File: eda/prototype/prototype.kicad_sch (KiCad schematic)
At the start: 9 parts, among them U1 8088_Min_Mode, U2 GAL16V8, U3 74HC161, U4 74HC574, U5 SST39SF040, U6 HM62256BLP, U7 HM62256BLP, U8 74HC245, X1 CXO_DIP8

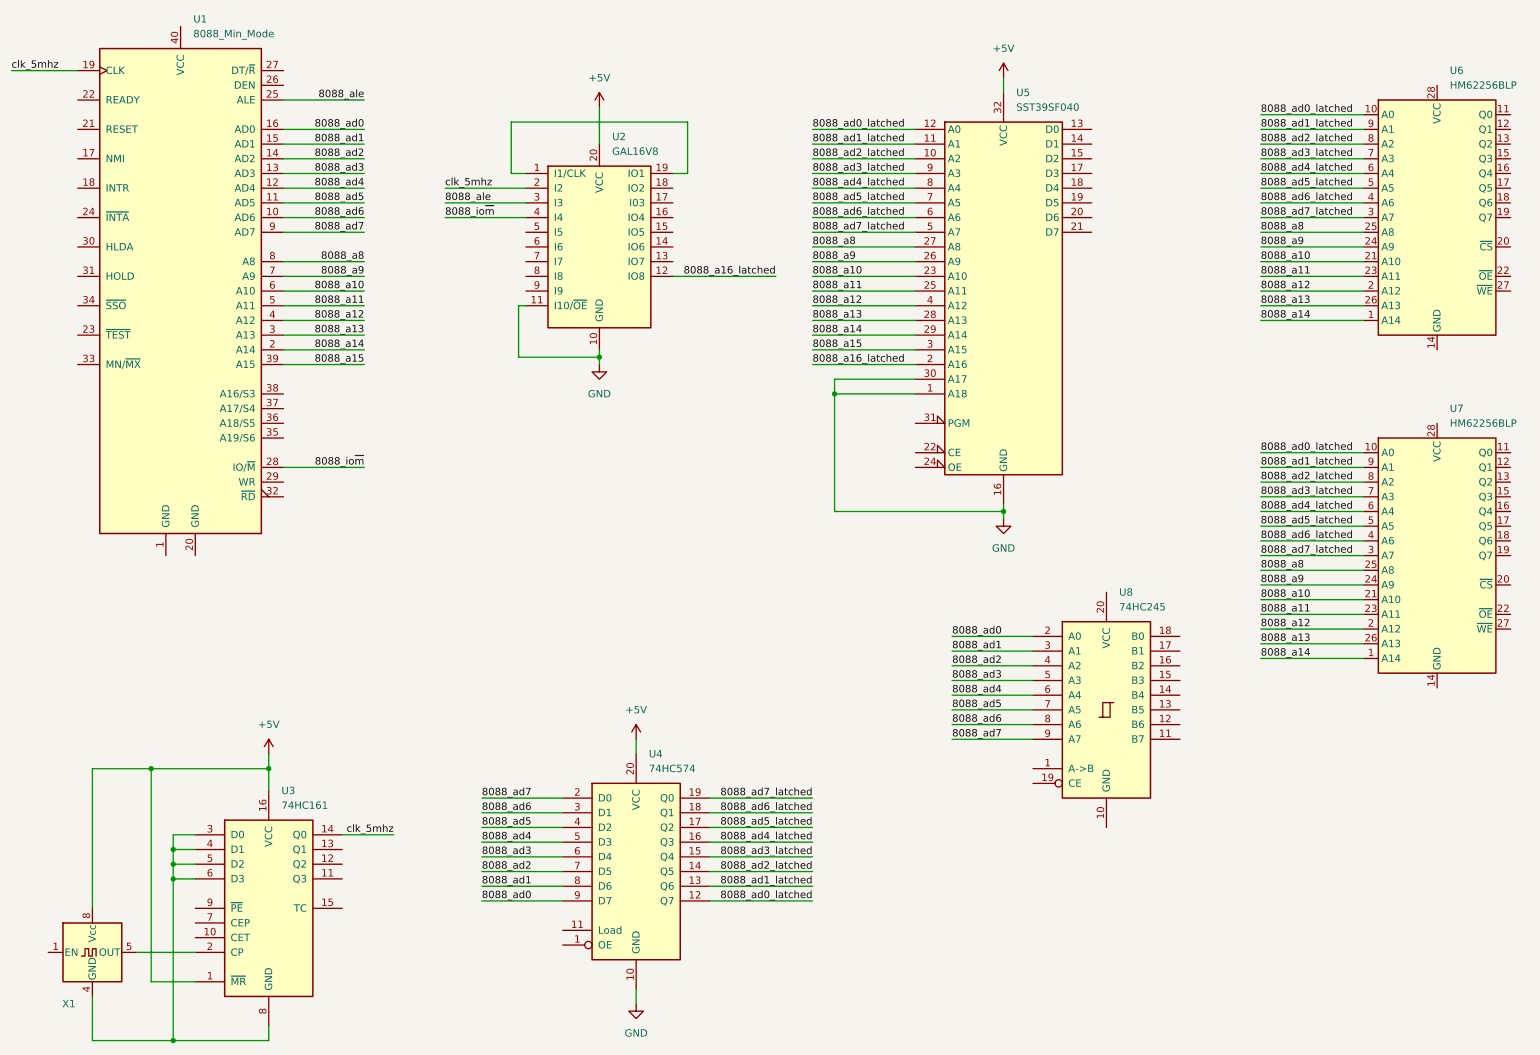
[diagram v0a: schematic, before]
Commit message: eda: Mostly complete prototype schematic
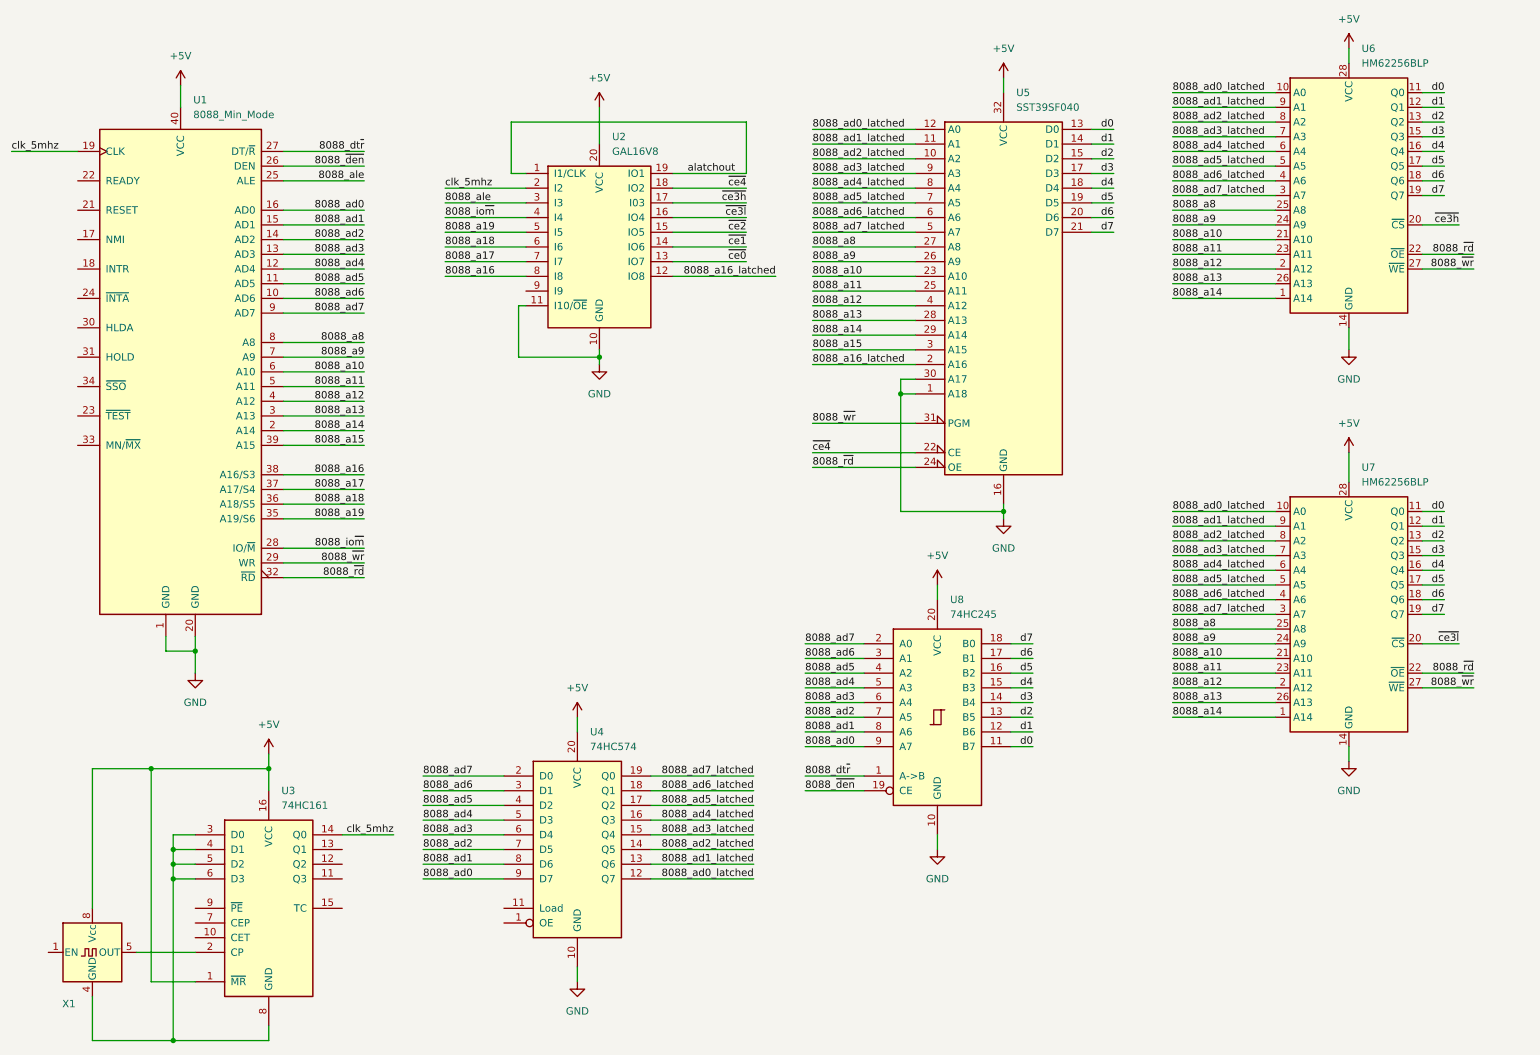
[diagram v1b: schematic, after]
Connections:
- net +5V: now also U1.40 (VCC), U6.28 (VCC), U7.28 (VCC), U8.20 (VCC)
- net 8088_ad0: now also U8.9 (A7); no longer U8.2 (A0)
- net 8088_ad1: now also U8.8 (A6); no longer U8.3 (A1)
- net 8088_ad2: now also U8.7 (A5); no longer U8.4 (A2)
- net 8088_ad3: now also U8.6 (A4); no longer U8.5 (A3)
- net 8088_ad4: now also U8.5 (A3); no longer U8.6 (A4)
- net 8088_ad5: now also U8.4 (A2); no longer U8.7 (A5)
- net 8088_ad6: now also U8.3 (A1); no longer U8.8 (A6)
- net 8088_ad7: now also U8.2 (A0); no longer U8.9 (A7)
- net GND: now also U1.1 (GND), U1.20 (GND), U6.14 (GND), U7.14 (GND), U8.10 (GND)
- net d0: now reaches U5.13 (D0)
- net d0: now also U6.11 (Q0), U7.11 (Q0), U8.11 (B7)
- net d1: now reaches U5.14 (D1)
- net d1: now also U6.12 (Q1), U7.12 (Q1), U8.12 (B6)
- net d2: now reaches U5.15 (D2)
- net d2: now also U6.13 (Q2), U7.13 (Q2), U8.13 (B5)
- net d3: now reaches U5.17 (D3)
- net d3: now also U6.15 (Q3), U7.15 (Q3), U8.14 (B4)
- net d4: now reaches U5.18 (D4)
- net d4: now also U6.16 (Q4), U7.16 (Q4), U8.15 (B3)
- net d5: now reaches U5.19 (D5)
- net d5: now also U6.17 (Q5), U7.17 (Q5), U8.16 (B2)
- net d6: now reaches U5.20 (D6)
- net d6: now also U6.18 (Q6), U7.18 (Q6), U8.17 (B1)
- net d7: now reaches U5.21 (D7)
- net d7: now also U6.19 (Q7), U7.19 (Q7), U8.18 (B0)
- net ~{ce4}: now reaches U5.22 (CE)
- net ~{ce4}: now also U2.18 (IO2)
- net 8088_~{rd}: now reaches U5.24 (OE)
- net 8088_~{rd}: now also U1.32 (~{RD}), U6.22 (~{OE}), U7.22 (~{OE})
- net 8088_~{wr}: now reaches U5.31 (PGM)
- net 8088_~{wr}: now also U1.29 (WR), U6.27 (~{WE}), U7.27 (~{WE})
- net 8088_dt~{r}: now reaches U8.1 (A->B)
- net 8088_dt~{r}: now also U1.27 (DT/~{R})
- net 8088_~{den}: now reaches U8.19 (CE)
- net 8088_~{den}: now also U1.26 (DEN)
- net alatchout: now reaches U2.1 (I1/CLK), U2.19 (IO1)
- net ~{ce0}: now reaches U2.13 (IO7)
- net ~{ce1}: now reaches U2.14 (IO6)
- net ~{ce2}: now reaches U2.15 (IO5)
- net ~{ce3l}: now reaches U2.16 (IO4)
- net ~{ce3l}: now also U7.20 (~{CS})
- net ~{ce3h}: now reaches U2.17 (I03)
- net ~{ce3h}: now also U6.20 (~{CS})
- net 8088_a19: now reaches U2.5 (I5)
- net 8088_a19: now also U1.35 (A19/S6)
- net 8088_a18: now reaches U2.6 (I6)
- net 8088_a18: now also U1.36 (A18/S5)
- net 8088_a17: now reaches U2.7 (I7)
- net 8088_a17: now also U1.37 (A17/S4)
- net 8088_a16: now reaches U2.8 (I8)
- net 8088_a16: now also U1.38 (A16/S3)
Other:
- moved on the sheet: U1, U4, U6, U7, U8

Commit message: eda: prototype: bit more filling out
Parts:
- added R1, R2, R3, R4, R5, R6, R7: R, symbol Device:R
- added U9: GAL16V8, symbol Logic_Programmable:GAL16V8
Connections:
- net +5V: now also R3.1, R4.1, R7.1, U9.20 (VCC)
- net 8088_a12: now also U9.3 (I3)
- net 8088_a13: now also U9.4 (I4)
- net 8088_a14: now also U9.5 (I5)
- net 8088_a15: now also U9.6 (I6)
- net 8088_io~{m}: now also U9.2 (I2)
- net GND: now also U4.1 (OE), R1.1, R2.2, R5.2, R6.2, U9.10 (GND), U9.11 (I10/~{OE})
- net alatchout: now also U4.11 (Load), U9.1 (I1/CLK)
- net at U1.17 (NMI): now also R1.2
- net at U1.18 (INTR): now also R6.1
- net at U1.21 (RESET): now also R4.2
- net at U1.22 (READY): now also R7.2
- net at U1.23 (~{TEST}): now also R5.1
- net at U1.31 (HOLD): now also R2.1
- net at U1.33 (MN/~{MX}): now also R3.2
- new net ~{ioce0}: U9.12 (IO8)
- new net ~{ioce1}: U9.13 (IO7)
- new net ~{ioce2}: U9.14 (IO6)
- new net ~{ioce3}: U9.15 (IO5)
- new net ~{ioce4}: U9.16 (IO4)
- new net ~{ioce5}: U9.17 (I03)
- new net ~{ioce6}: U9.18 (IO2)
- new net ~{ioce7}: U9.19 (IO1)
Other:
- moved on the sheet: U1, U2, U4, U5, U6, U7, U8

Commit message: eda: prototype: Add pio
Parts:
- added U10: 8255A, Package_DIP:DIP-40_W15.24mm, symbol Interface:8255A
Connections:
- net ~{ioce7} is gone; now on net 8088_io~{m}: U9.19 (IO1)
- net 8088_a12: now also U9.6 (I6); no longer U9.3 (I3)
- net 8088_a13: now also U9.7 (I7); no longer U9.4 (I4)
- net 8088_a14: now also U9.8 (I8); no longer U9.5 (I5)
- net 8088_a15: now also U9.9 (I9); no longer U9.6 (I6)
- net 8088_ad0_latched: now also U10.8 (A1)
- net 8088_ad1_latched: now also U10.9 (A0)
- net 8088_ad4: now also U9.5 (I5)
- net 8088_ad5: now also U9.4 (I4)
- net 8088_ad6: now also U9.3 (I3)
- net 8088_ad7: now also U9.2 (I2)
- net 8088_io~{m}: no longer U9.2 (I2)
- net 8088_~{rd}: now also U10.5 (~{RD})
- net 8088_~{wr}: now also U10.36 (~{WR})
- net GND: now also U10.7 (GND)
- net d0: now also U10.34 (D0)
- net d1: now also U10.33 (D1)
- net d2: now also U10.32 (D2)
- net d3: now also U10.31 (D3)
- net d4: now also U10.30 (D4)
- net d5: now also U10.29 (D5)
- net d6: now also U10.28 (D6)
- net d7: now also U10.27 (D7)
- net ~{ioce0}: now also U10.6 (~{CS})
- net reset: now reaches R4.2, U1.21 (RESET)
- net reset: now also U10.35 (RESET)
- net ~{ioce6} renamed ~{iodbg}
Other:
- moved on the sheet: U9

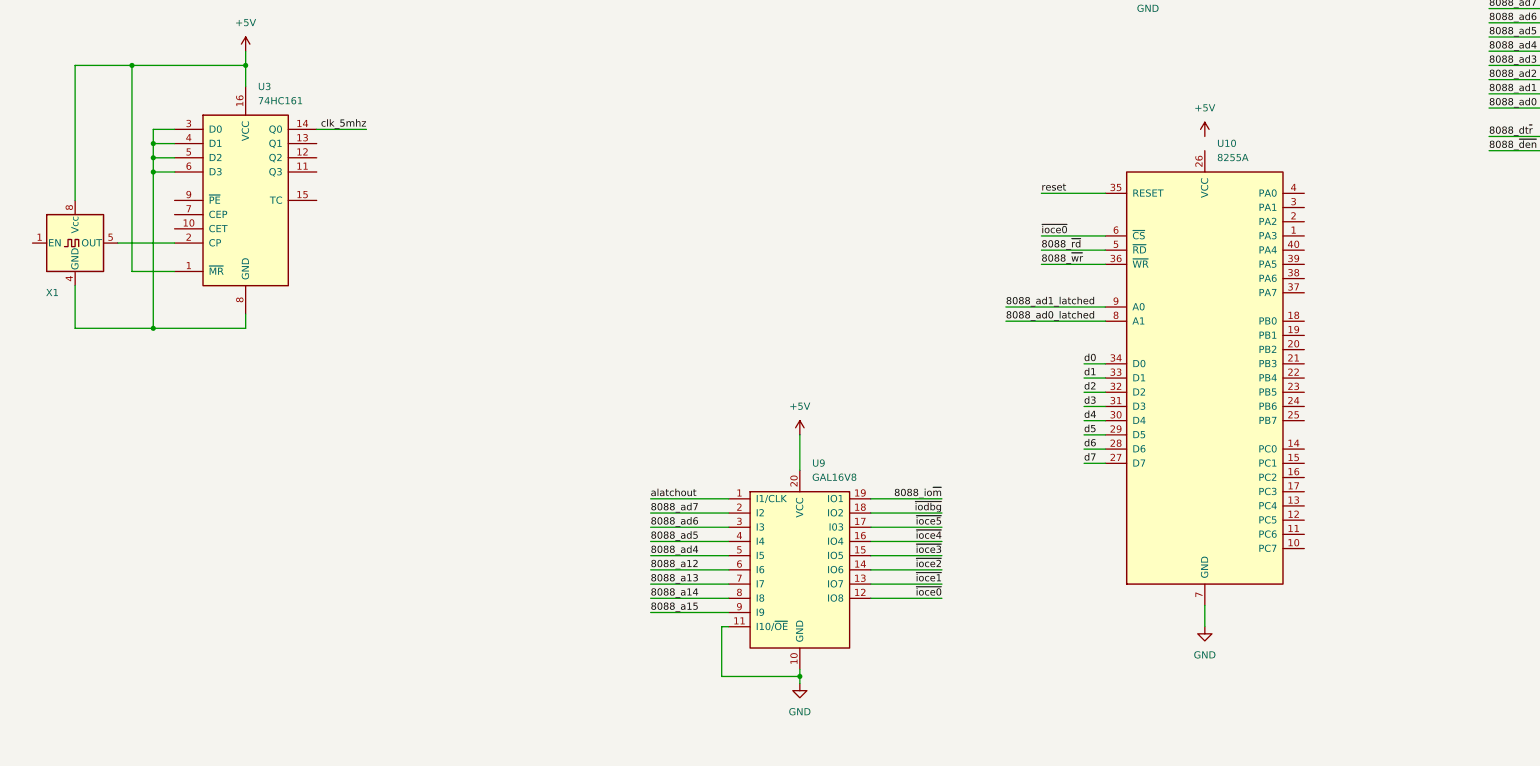
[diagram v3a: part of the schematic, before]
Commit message: eda: prototype: Update schematic
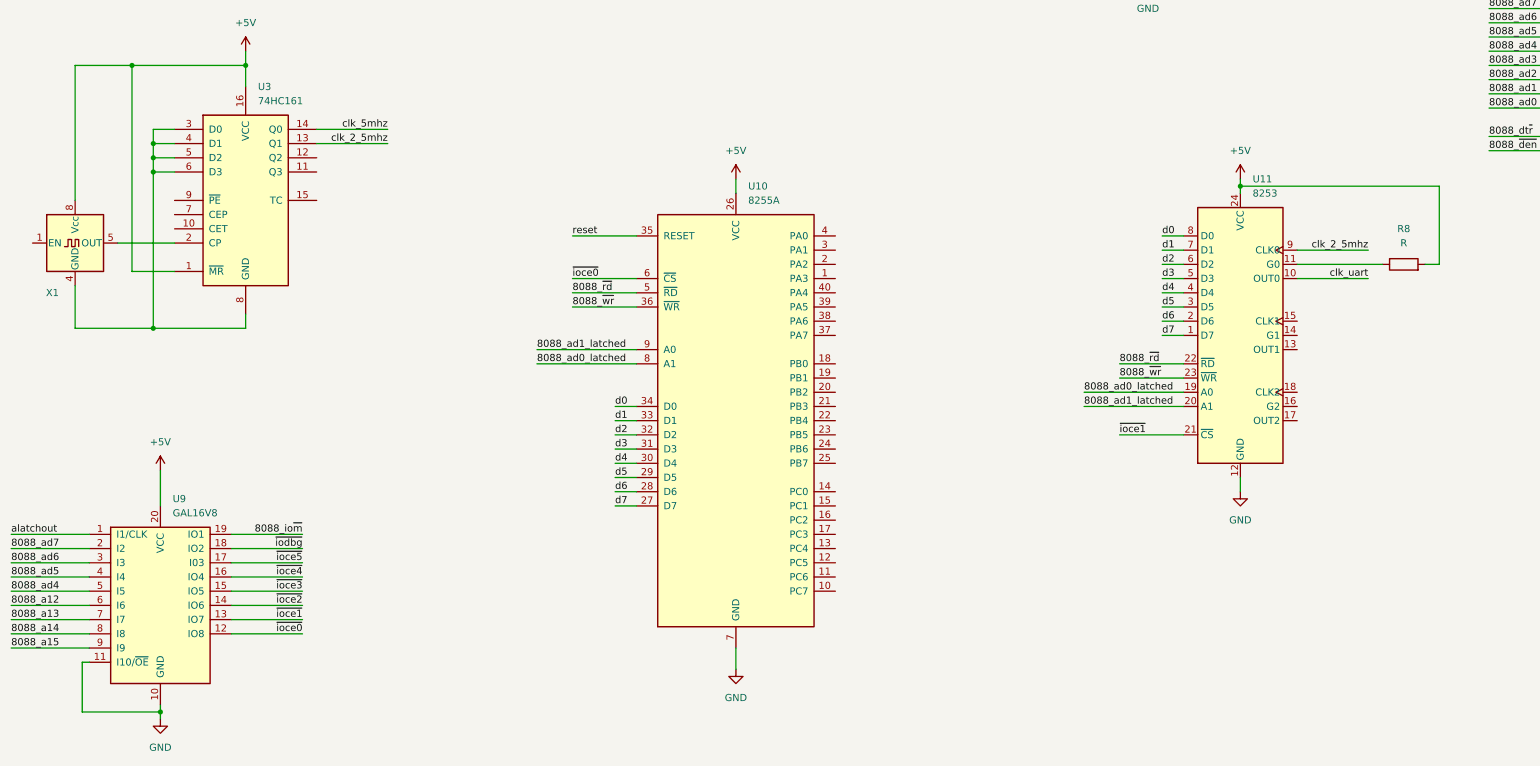
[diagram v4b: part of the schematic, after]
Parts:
- added R8: R, symbol Device:R
- added U11: 8253, Package_DIP:DIP-24_W15.24mm, symbol Timer:8253
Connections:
- net +5V: now also U10.26 (VCC), R8.2, U11.24 (VCC)
- net 8088_ad0_latched: now also U11.19 (A0)
- net 8088_ad1_latched: now also U11.20 (A1)
- net 8088_~{rd}: now also U11.22 (~{RD})
- net 8088_~{wr}: now also U11.23 (~{WR})
- net GND: now also U11.12 (GND)
- net d0: now also U11.8 (D0)
- net d1: now also U11.7 (D1)
- net d2: now also U11.6 (D2)
- net d3: now also U11.5 (D3)
- net d4: now also U11.4 (D4)
- net d5: now also U11.3 (D5)
- net d6: now also U11.2 (D6)
- net d7: now also U11.1 (D7)
- net ~{ioce1}: now also U11.21 (~{CS})
- net clk_2_5mhz: now reaches U3.13 (Q1)
- net clk_2_5mhz: now also U11.9 (CLK0)
- new net: R8.1, U11.11 (G0)
- new net clk_uart: U11.10 (OUT0)
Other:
- moved on the sheet: U10, U9

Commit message: eda: prototype: Add PIC
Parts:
- added R10, R11, R12, R13, R14, R15, R16, R9: R, symbol Device:R
- added U12: 8259A, Package_DIP:DIP-28_W15.24mm, symbol Interface:8259A
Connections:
- net +5V: now also U12.28 (VCC)
- net GND: now also R10.2, R11.2, R12.2, R13.2, R14.2, R15.2, R16.2, R9.2, U12.14 (GND)
- net d0: now also U12.11 (D0)
- net d1: now also U12.10 (D1)
- net d2: now also U12.9 (D2)
- net d3: now also U12.8 (D3)
- net d5: now also U12.6 (D5)
- net d7: now also U12.4 (D7)
- net 8088_intr: now reaches R6.1, U1.18 (INTR)
- net 8088_intr: now also U12.17 (INT)
- net 8088_~{inta}: now reaches U1.24 (~{INTA})
- net 8088_~{inta}: now also U12.26 (~{INTA})
- new net: R15.1, U12.24 (IR6)
- new net: R9.1, U12.18 (IR0)
- new net: R12.1, U12.21 (IR3)
- new net: R10.1, U12.19 (IR1)
- new net: R11.1, U12.20 (IR2)
- new net: R13.1, U12.22 (IR4)
- new net: R14.1, U12.23 (IR5)
- new net: R16.1, U12.25 (IR7)
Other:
- note added: "note: this is 50% duty cycle which is "wrong" but works :D"
- moved on the sheet: R8, U11, U8

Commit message: eda: prototype: Add usart
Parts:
- added J1: Conn_02x05_Odd_Even, symbol Connector_Generic:Conn_02x05_Odd_Even
- added R17, R18, R19, R20, R21: R, symbol Device:R
- added U13: 8251, symbol 82xx:8251
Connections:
- net +5V: now also R17.1, R18.2, R19.2, U13.26 (VCC)
- net 8088_ad0_latched: now also U12.27 (A0), U13.12 (C/~{D})
- net 8088_~{rd}: now also U12.3 (~{RD}), U13.13 (~{RD})
- net 8088_~{wr}: now also U12.2 (~{WR}), U13.10 (~{WR})
- net GND: now also J1.5 (Pin_5), R20.2, R21.2, U13.4 (GND)
- net clk_2_5mhz: now also U13.20 (CLK)
- net clk_uart: now also U13.25 (~{RxC}), U13.9 (~{TxC})
- net d0: now also U13.27 (D0)
- net d1: now also U13.28 (D1)
- net d2: now also U13.1 (D2)
- net d3: now also U13.2 (D3)
- net d4: now also U12.7 (D4), U13.5 (D4)
- net d5: now also U13.6 (D5)
- net d6: now also U12.5 (D6), U13.7 (D6)
- net d7: now also U13.8 (D7)
- net reset: now also U13.21 (RES)
- net ~{ioce2}: now also U13.11 (~{CS})
- net ~{ioce3}: now also U12.1 (~{CS})
- net usart_break_detect: now reaches R1.2, U1.17 (NMI)
- net usart_break_detect: now also U13.16 (SYNDET/BD)
- net at U12.16 (~{SP}/~{EN}): now also R17.2
- net int_tick: now reaches R10.1, U12.19 (IR1)
- net int_tick: now also U11.13 (OUT1)
- net int_usart_rxrdy: now reaches R11.1, U12.20 (IR2)
- net int_usart_rxrdy: now also U13.14 (RxRDY)
- net int_usart_txrdy: now reaches R14.1, U12.23 (IR5)
- net int_usart_txrdy: now also U13.15 (TxRDY)
- net at U11.14 (G1): now also R18.1
- net clk_0_625mhz: now reaches U11.15 (CLK1)
- net clk_0_625mhz: now also U3.11 (Q3)
- net at U11.16 (G2): now also R19.1
- net clk_1_25mhz: now reaches U11.18 (CLK2)
- net clk_1_25mhz: now also U3.12 (Q2)
- new net: R21.1, U13.22 (~{DSR})
- new net: R20.1, U13.17 (~{CTS})
- new net usart_rx: J1.2 (Pin_2), U13.3 (RxD)
- new net usart_tx: J1.3 (Pin_3), U13.19 (TxD)
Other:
- moved on the sheet: R10, R11, R12, R13, R14, R15, R16, R8, R9, U10, U11, U12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
